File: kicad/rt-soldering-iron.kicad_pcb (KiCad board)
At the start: 2 copper layers, 87.6 x 20.3 mm, 83 parts, among them J1 IRON_TIP, J2 BARREL_JACK, J3 CONN_01X04, Q1 SIA483DJ-T1-GE3, Q2 MMBT3904, SW1 JS5208, U1 ACS711xEX, U2 OPA188AIDBV, U3 AP3211, U4 STM32F031G, U5 SSD1306-OLED-I2C, U6 MMA8652FC

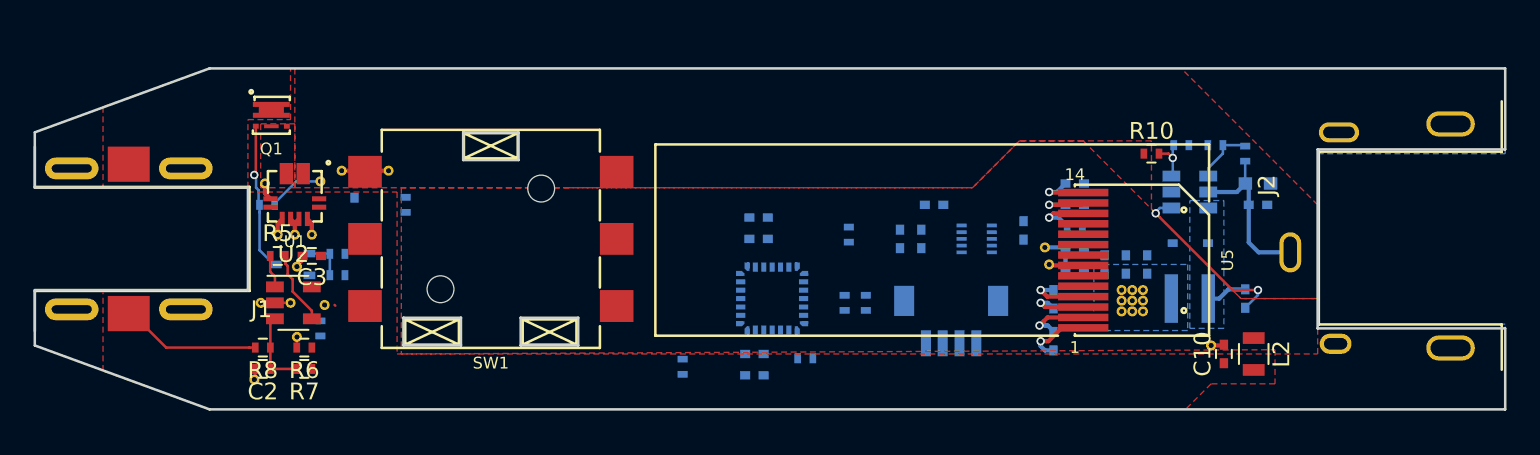
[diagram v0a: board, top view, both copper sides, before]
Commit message: Added buzzer, fixed footprint errors, and updated silkscreen
The board is probably ready to be ordered
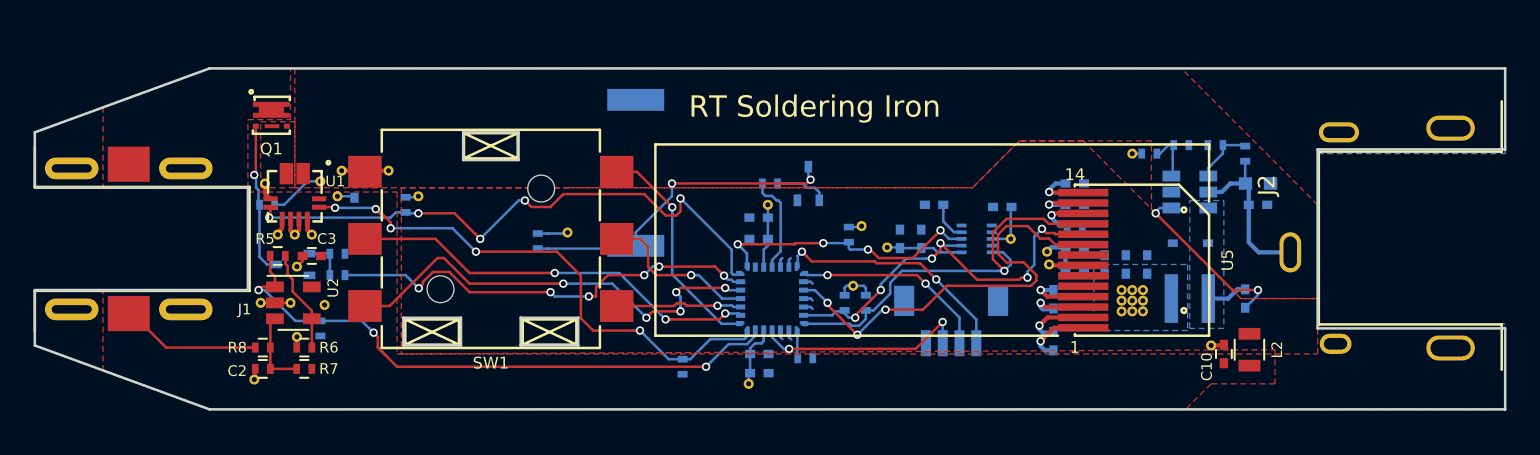
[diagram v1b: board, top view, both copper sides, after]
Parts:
- added LS1: PKMCS0909E4000, rt-soldering-iron:Murata-PKMCS, B.Cu at (139.7, 92.6)
- added Q3: MMBT3904, TO_SOT_Packages_SMD:SOT-323_SC-70, B.Cu at (150.0, 93.2)
- added R19: 270, Resistors_SMD:R_0402, B.Cu at (133.9, 96.6)
- added R20: 1K, Resistors_SMD:R_0402, B.Cu at (147.7, 93.2)
- added REF**: 1PIN-VIA, rt-soldering-iron:1PIN-VIA, F.Cu at (135.6, 96.1)
- added REF**: 1PIN-VIA, rt-soldering-iron:1PIN-VIA, F.Cu at (162.1, 96.5)
- added REF**: 1PIN-VIA, rt-soldering-iron:1PIN-VIA, F.Cu at (169.3, 91.4)
- added REF**: 1PIN-VIA, rt-soldering-iron:1PIN-VIA, F.Cu at (121.9, 94.0)
- added REF**: 1PIN-VIA, rt-soldering-iron:1PIN-VIA, F.Cu at (126.7, 94.0)
- added REF**: 1PIN-VIA, rt-soldering-iron:1PIN-VIA, F.Cu at (152.7, 99.3)
- added REF**: 1PIN-VIA, rt-soldering-iron:1PIN-VIA, F.Cu at (146.4, 105.2)
- added REF**: 1PIN-VIA, rt-soldering-iron:1PIN-VIA, F.Cu at (147.6, 94.5)
- added REF**: 1PIN-VIA, rt-soldering-iron:1PIN-VIA, F.Cu at (153.2, 95.8)
- added REF**: 1PIN-VIA, rt-soldering-iron:1PIN-VIA, F.Cu at (154.7, 97.0)
- R10: moved to B.Cu
- moved C23 1.89 mm to (161.5, 94.6), turned to 180 degrees
- moved L2 0.36 mm to (176.3, 103.1)
- moved C14 0.32 mm to (147.1, 104.5), turned to 0 degrees
- moved C13 0.30 mm to (147.1, 103.4), turned to 0 degrees
- moved REF** 0.28 mm to (164.2, 97.3)
- moved R10 0.13 mm to (170.3, 91.4)
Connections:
- U4 pad 18: Net-(U4-Pad18) -> /Digital Control/BUZ_CTL
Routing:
- net /Analog Frontend/~FAULT: track 0.00 -> 35.0 mm, vias 0 -> 5
- net /Analog Frontend/HEATER_SENSE: track 1.96 -> 36.7 mm, vias 0 -> 3
- net /Analog Frontend/CURRENT_SENSE: track 0.00 -> 32.0 mm, vias 0 -> 5
- net /Digital Control/SW_E: track 0.00 -> 26.9 mm, vias 0 -> 5
- net /Analog Frontend/HEATER_CTL: track 0.00 -> 26.4 mm, vias 0 -> 6
- net /Digital Control/~OLED_RST: track 0.00 -> 26.4 mm, vias 0 -> 3
- net /Digital Control/SW_B: track 0.00 -> 24.6 mm, vias 0 -> 3
- net /Digital Control/I2C_SDA: track 0.00 -> 24.5 mm, vias 0 -> 1
- net /Digital Control/I2C_SCL: track 0.00 -> 24.2 mm, vias 0 -> 6
- net /Digital Control/BUZ_COL: track 0.00 -> 19.7 mm, vias 0 -> 2
- net +3V3: track 2.50 -> 20.1 mm
- net /Digital Control/ACC_INT: track 0.00 -> 16.4 mm, vias 0 -> 4
- net /Digital Control/STM32_SWDIO: track 0.00 -> 14.4 mm, vias 0 -> 2
- net /Digital Control/SW_A: track 0.00 -> 13.4 mm, vias 0 -> 1
- net /Digital Control/~STM32_RESET: track 0.00 -> 12.8 mm, vias 0 -> 2
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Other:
- rule pad_to_mask_clearance: 0.1524 -> 0.07366
- board text added: "2017 Rev A"
- board text added: "Kevin Cuzner"
- board text added: "RT Soldering Iron"

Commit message: Changed out the op amp and fixed oval holes for OSHPark
I don't think I'm going to go with OSHPark. It seems they can't
fabricate this thing.
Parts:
- removed the REF** at (121.2, 100.5)
- removed the REF** at (119.1, 100.3)
- added C26: SPR, Capacitors_SMD:C_0402, F.Cu at (121.7, 103.6)
- added D2: BAS70-04W, TO_SOT_Packages_SMD:SOT-323_SC-70, B.Cu at (117.6, 103.0)
- added REF**: 1PIN-VIA, rt-soldering-iron:1PIN-VIA, F.Cu at (115.8, 102.4)
- U2: value OPA188AIDBV -> MCP6V71U; footprint TO_SOT_Packages_SMD:SOT-23-5 -> TO_SOT_Packages_SMD:SOT-353_SC-70-5
- turned R5 to 180 degrees
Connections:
- U2 pad 1: /Analog Frontend/HEATER_SENSE -> /Analog Frontend/OPAMP_FB
- U2 pad 4: /Analog Frontend/OPAMP_FB -> /Analog Frontend/HEATER_SENSE
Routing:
- net /Analog Frontend/OPAMP_FB: track 6.12 -> 9.47 mm
- net /Analog Frontend/OPAMP_SENSE_IN: track 4.67 -> 6.33 mm, vias 0 -> 1
- net +3.3VA: track 4.86 -> 5.65 mm
- net GND: track 14.9 -> 14.1 mm
- net /Analog Frontend/SENSE_IN: track 8.38 -> 9.13 mm
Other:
- outline, holes or cut-outs redrawn

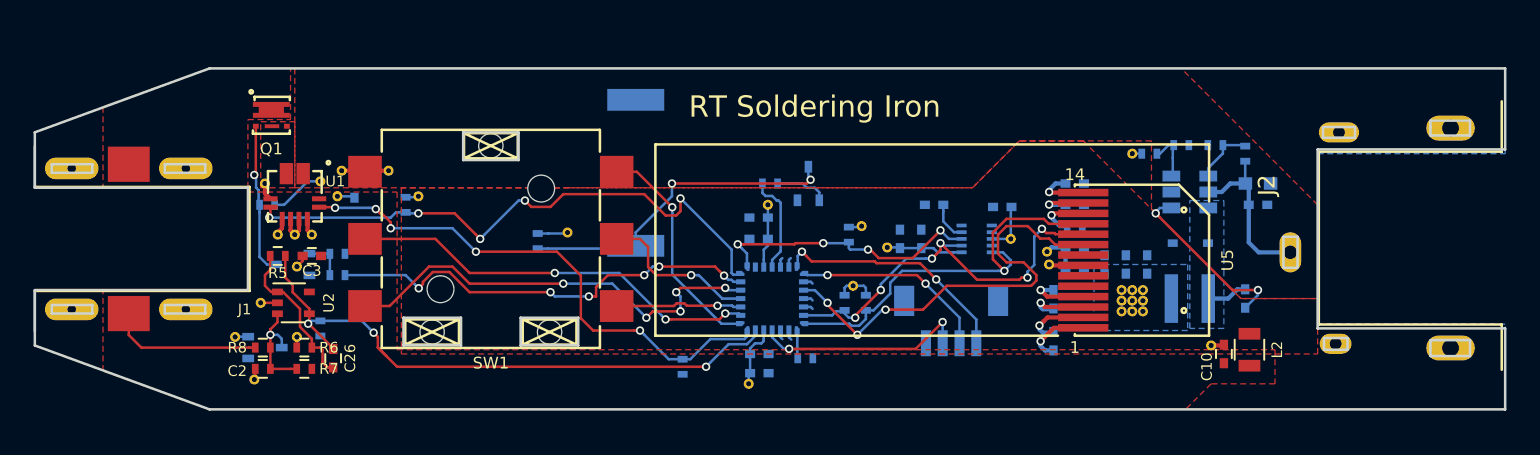
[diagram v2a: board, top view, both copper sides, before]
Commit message: Removed comp, efuse. Added zener protection. Fixed OLED footprint.
I may have destroyed a board by shorting the FB pin to ground. I left
off the zener protection on Rev A. Never again.
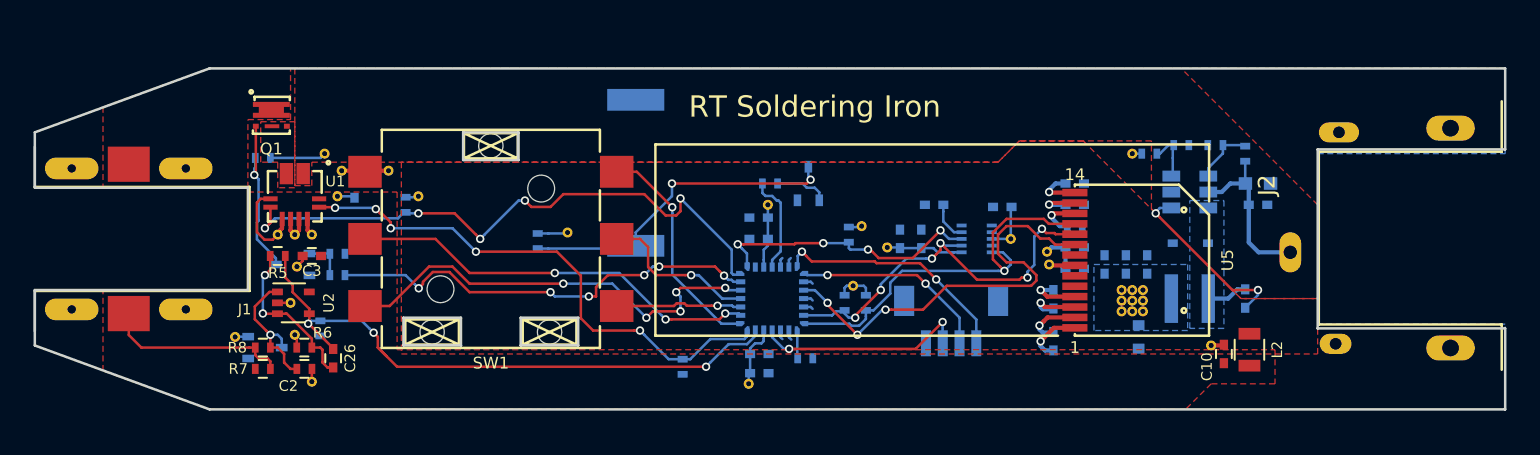
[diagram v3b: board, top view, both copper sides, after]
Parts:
- removed the REF** at (117.6, 93.2)
- added D3: 3.6V, Diodes_SMD:D_SOD-523, B.Cu at (169.7, 102.4)
- moved REF** 3.43 mm to (120.4, 105.0)
- moved R2 2.81 mm to (117.5, 91.7)
- moved C2 2.48 mm to (120.0, 104.3), turned to 0 degrees
- moved R7 2.47 mm to (117.5, 104.3), turned to 0 degrees
- moved REF** 1.78 mm to (119.1, 100.3)
- moved REF** 1.67 mm to (121.2, 91.4)
- moved REF** 0.18 mm to (119.4, 102.2)
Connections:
- net Net-(U4-Pad19) renamed /Digital Control/~HEATER_EN
- R7 pad 2: /Analog Frontend/OPAMP_SENSE_IN -> /Analog Frontend/SENSE_IN
- U2 pad 1: /Analog Frontend/OPAMP_FB -> /Analog Frontend/OPAMP_SENSE_IN
- U2 pad 3: /Analog Frontend/OPAMP_SENSE_IN -> /Analog Frontend/OPAMP_FB
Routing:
- net GND: track 14.1 -> 17.3 mm
- net /Analog Frontend/SENSE_IN: track 9.13 -> 11.1 mm
- net /Analog Frontend/OPAMP_SENSE_IN: track 6.33 -> 8.24 mm
- net /Analog Frontend/~FAULT: track 35.0 -> 36.3 mm
- net /Analog Frontend/TIP_GATE: track 9.12 -> 9.93 mm
- net /Analog Frontend/OPAMP_FB: track 9.47 -> 9.99 mm, vias 0 -> 2
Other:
- outline, holes or cut-outs redrawn
- board text added: "2017 Rev B"
- board text added: "Before sending gerbers, add edge cuts for the oval pins"
- board text removed: "2017 Rev A"

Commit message: Finished placement of all parts. Routed power supply.
The board has been shrunk by 10mm or so. The elimination of the giant
directional switch is the reason this is even possible.
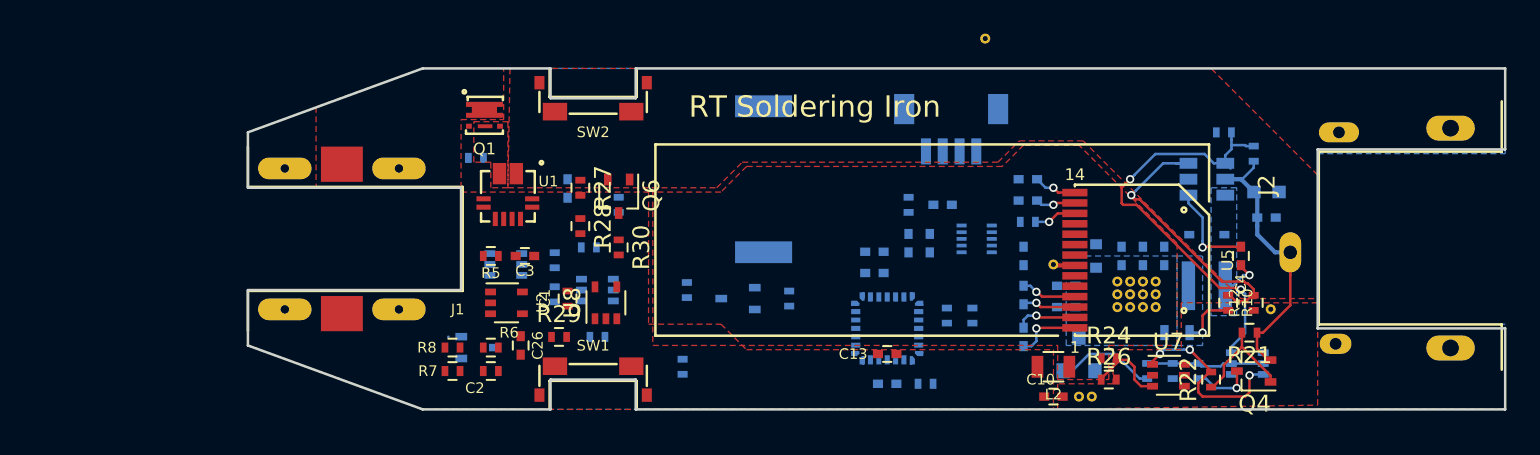
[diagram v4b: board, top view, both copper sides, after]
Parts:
- removed the REF** at (115.8, 102.4)
- removed the REF** at (154.7, 97.0)
- removed the REF** at (162.1, 96.5)
- removed the REF** at (164.2, 97.3)
- removed the REF** at (164.3, 98.0)
- removed the REF** at (169.9, 100.8)
- removed the REF** at (169.3, 100.8)
- removed the REF** at (168.7, 100.8)
- removed the REF** at (168.7, 100.2)
- removed the REF** at (169.3, 100.2)
- removed the REF** at (169.9, 100.2)
- removed the REF** at (135.6, 96.1)
- removed the REF** at (169.9, 99.6)
- removed the REF** at (168.7, 99.6)
- removed the REF** at (169.3, 99.6)
- removed the REF** at (174.0, 102.9)
- removed the REF** at (119.5, 98.2)
- removed the REF** at (119.1, 100.3)
- removed the REF** at (119.4, 102.2)
- removed the REF** at (120.4, 105.0)
- removed the REF** at (121.2, 91.4)
- removed the REF** at (120.4, 96.3)
- removed the REF** at (169.3, 91.4)
- removed the REF** at (119.4, 96.3)
- removed the REF** at (118.4, 96.3)
- removed the REF** at (122.2, 92.5)
- removed the REF** at (125.0, 92.5)
- removed the REF** at (121.9, 94.0)
- removed the REF** at (126.7, 94.0)
- removed the REF** at (152.7, 99.3)
- removed the REF** at (146.4, 105.2)
- removed the REF** at (147.6, 94.5)
- removed the REF** at (153.2, 95.8)
- added D4: Q_Thyristor_KGA, TO_SOT_Packages_SMD:SOT-23, B.Cu at (166.1, 103.4)
- added F1: Fuse_Small, Resistors_SMD:R_0603, B.Cu at (172.0, 102.1)
- added Q4: MMBT3906WT1G, TO_SOT_Packages_SMD:SOT-323_SC-70, F.Cu at (176.5, 104.4)
- added Q5: FDG6301N_F085, TO_SOT_Packages_SMD:SOT-363_SC-70-6, B.Cu at (176.1, 103.9)
- added Q6: MMBT3906WT1G, TO_SOT_Packages_SMD:SOT-323_SC-70, F.Cu at (138.7, 94.0)
- added Q7: FDG6301N_F085, TO_SOT_Packages_SMD:SOT-363_SC-70-6, B.Cu at (137.4, 99.6)
- added R21: 10K, Resistors_SMD:R_0402, F.Cu at (176.3, 102.1)
- added R22: 1K, Resistors_SMD:R_0402, F.Cu at (174.0, 104.9)
- added R23: 10K, Resistors_SMD:R_0402, B.Cu at (173.2, 104.4)
- added R24: 10K, Resistors_SMD:R_0402, F.Cu at (167.9, 103.6)
- added R25: 10K, Resistors_SMD:R_0402, B.Cu at (171.7, 104.4)
- added R26: 22K6, Resistors_SMD:R_0402, F.Cu at (167.9, 104.9)
- added R27: 10K, Resistors_SMD:R_0402, F.Cu at (136.4, 93.5)
- added R28: 1K, Resistors_SMD:R_0402, F.Cu at (136.4, 95.8)
- added R29: 16K2, Resistors_SMD:R_0402, F.Cu at (135.1, 102.4)
- added R30: 10K, Resistors_SMD:R_0402, F.Cu at (138.7, 97.0)
- added R31: 100K, Resistors_SMD:R_0402, B.Cu at (137.4, 102.4)
- added R32: 10K, Resistors_SMD:R_0402, B.Cu at (134.9, 99.8)
- added R33: 10K, Resistors_SMD:R_0402, B.Cu at (170.2, 104.4)
- added REF**: 1PIN-VIA, rt-soldering-iron:1PIN-VIA, F.Cu at (164.6, 98.0)
- added REF**: 1PIN-VIA, rt-soldering-iron:1PIN-VIA, F.Cu at (169.9, 99.8)
- added REF**: 1PIN-VIA, rt-soldering-iron:1PIN-VIA, F.Cu at (170.7, 99.8)
- added REF**: 1PIN-VIA, rt-soldering-iron:1PIN-VIA, F.Cu at (170.7, 99.1)
- added REF**: 1PIN-VIA, rt-soldering-iron:1PIN-VIA, F.Cu at (169.9, 99.1)
- added REF**: 1PIN-VIA, rt-soldering-iron:1PIN-VIA, F.Cu at (166.1, 105.9)
- added REF**: 1PIN-VIA, rt-soldering-iron:1PIN-VIA, F.Cu at (168.4, 99.1)
- added REF**: 1PIN-VIA, rt-soldering-iron:1PIN-VIA, F.Cu at (169.2, 99.1)
- added REF**: 1PIN-VIA, rt-soldering-iron:1PIN-VIA, F.Cu at (160.5, 84.6)
- added REF**: 1PIN-VIA, rt-soldering-iron:1PIN-VIA, F.Cu at (177.5, 100.7)
- added REF**: 1PIN-VIA, rt-soldering-iron:1PIN-VIA, F.Cu at (166.9, 105.9)
- added REF**: 1PIN-VIA, rt-soldering-iron:1PIN-VIA, F.Cu at (170.7, 100.6)
- added REF**: 1PIN-VIA, rt-soldering-iron:1PIN-VIA, F.Cu at (169.9, 100.6)
- added REF**: 1PIN-VIA, rt-soldering-iron:1PIN-VIA, F.Cu at (169.2, 100.6)
- added REF**: 1PIN-VIA, rt-soldering-iron:1PIN-VIA, F.Cu at (168.4, 100.6)
- added REF**: 1PIN-VIA, rt-soldering-iron:1PIN-VIA, F.Cu at (168.4, 99.8)
- added REF**: 1PIN-VIA, rt-soldering-iron:1PIN-VIA, F.Cu at (169.2, 99.8)
- added SW2: SPST, rt-soldering-iron:Panasonic_EVQP4, F.Cu at (137.2, 86.4)
- added U7: TL431, TO_SOT_Packages_SMD:SOT-363_SC-70-6, F.Cu at (171.4, 104.6)
- added U8: TLV1701, TO_SOT_Packages_SMD:SOT-353_SC-70-5, F.Cu at (137.9, 100.3)
- C1, C13, C4, R10, R12: moved to F.Cu
- Q2: value MMBT3904 -> FDG6301N_F085; footprint TO_SOT_Packages_SMD:SOT-323_SC-70 -> TO_SOT_Packages_SMD:SOT-363_SC-70-6
- SW1: value JS5208 -> SPST; footprint rt-soldering-iron:JS5208 -> rt-soldering-iron:Panasonic_EVQP4
- moved R3 15.1 mm to (136.9, 97.0)
- moved C1 14.8 mm to (135.6, 100.1), turned to 90 degrees
- moved R4 13.0 mm to (134.9, 97.8), turned to 90 degrees
- moved R2 12.7 mm to (130.2, 91.7)
- moved U1 12.7 mm to (132.1, 94.0)
- moved C3 12.7 mm to (133.1, 97.5)
- moved J1 12.7 mm to (116.6, 96.5)
- moved Q2 12.7 mm to (132.0, 98.0), turned to 0 degrees
- moved R1 12.7 mm to (138.7, 94.5)
- moved U2 12.7 mm to (132.0, 100.3)
- moved C25 12.7 mm to (135.6, 93.5)
- moved D2 12.7 mm to (130.3, 103.0)
- moved Q1 12.7 mm to (130.7, 89.2)
- moved R5 12.7 mm to (131.1, 97.5)
- moved SW1 11.8 mm to (137.2, 106.7)
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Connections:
- net /Digital Control/~HEATER_EN renamed Net-(U4-Pad19)
- net Net-(R11-Pad1) renamed /Power Supplies/+3.3V_EN
- L1 pad 2: +3V3 -> /Power Supplies/+3.3V_PREFUSE
- Q2 pad 1: /Analog Frontend/TIP_GATE_B -> GND
- Q2 pad 2: GND -> /Analog Frontend/HEATER_LATCH_RESET
- R10 pad 1: +3V3 -> /Power Supplies/+3.3V_PREFUSE
- SW1 pad 2: /Digital Control/SW_B -> /Digital Control/SW_A
- SW1 pad 3: /Digital Control/SW_E -> (no net)
- SW1 pad 4: /Digital Control/SW_A -> (no net)
- U4 pad 10: /Digital Control/SW_C -> Net-(U4-Pad10)
- U4 pad 11: /Digital Control/SW_D -> Net-(U4-Pad11)
- U4 pad 12: /Digital Control/SW_E -> Net-(U4-Pad12)
- U4 pad 25: Net-(U4-Pad25) -> /Analog Frontend/HEATER_LATCH_RESET
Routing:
- net /Analog Frontend/HEATER_SENSE: track 36.9 -> 0.00 mm, vias 3 -> 0
- net /Analog Frontend/~FAULT: track 36.3 -> 0.00 mm, vias 5 -> 0
- net /Analog Frontend/CURRENT_SENSE: track 32.0 -> 0.00 mm, vias 5 -> 0
- net /Digital Control/SW_E: track 26.4 -> 0.00 mm, vias 5 -> 0
- net /Analog Frontend/HEATER_CTL: track 26.4 -> 0.00 mm, vias 6 -> 0
- net /Digital Control/~OLED_RST: track 26.4 -> 0.00 mm, vias 3 -> 0
- net /Digital Control/SW_B: track 24.6 -> 0.00 mm, vias 3 -> 0
- net /Digital Control/I2C_SDA: track 24.5 -> 0.00 mm, vias 1 -> 0
- net /Digital Control/I2C_SCL: track 24.2 -> 0.00 mm, vias 6 -> 0
- net /Power Supplies/+3.3V_EN: track 3.56 -> 25.4 mm, vias 0 -> 2
- net +3V3: track 20.1 -> 0.00 mm
- net /Digital Control/BUZ_COL: track 19.7 -> 0.00 mm, vias 2 -> 0
- net /Digital Control/ACC_INT: track 16.4 -> 0.00 mm, vias 4 -> 0
- net GND: track 17.3 -> 1.30 mm
- net /Digital Control/STM32_SWDIO: track 14.4 -> 0.00 mm, vias 2 -> 0
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- added copper zone on B.Cu, net /Power Supplies/+3.3V_PREFUSE
- added copper zone on F.Cu, net GND
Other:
- board size 87.6 x 20.3 mm -> 74.9 x 20.3 mm
